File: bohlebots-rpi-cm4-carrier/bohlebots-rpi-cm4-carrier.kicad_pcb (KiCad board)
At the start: 2 copper layers, 132 x 132 mm, 41 parts, among them J1 SI-46001-F, J2 power_reference, J3 IO_Conn_02x05, J4 I2C_Conn_1x04, J5 pwr_connector, J6 pwr_connector, K1 Kicker, T1 Taster_LED, T2 Taster_LED, U1 Compute_Module_4_Connectors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

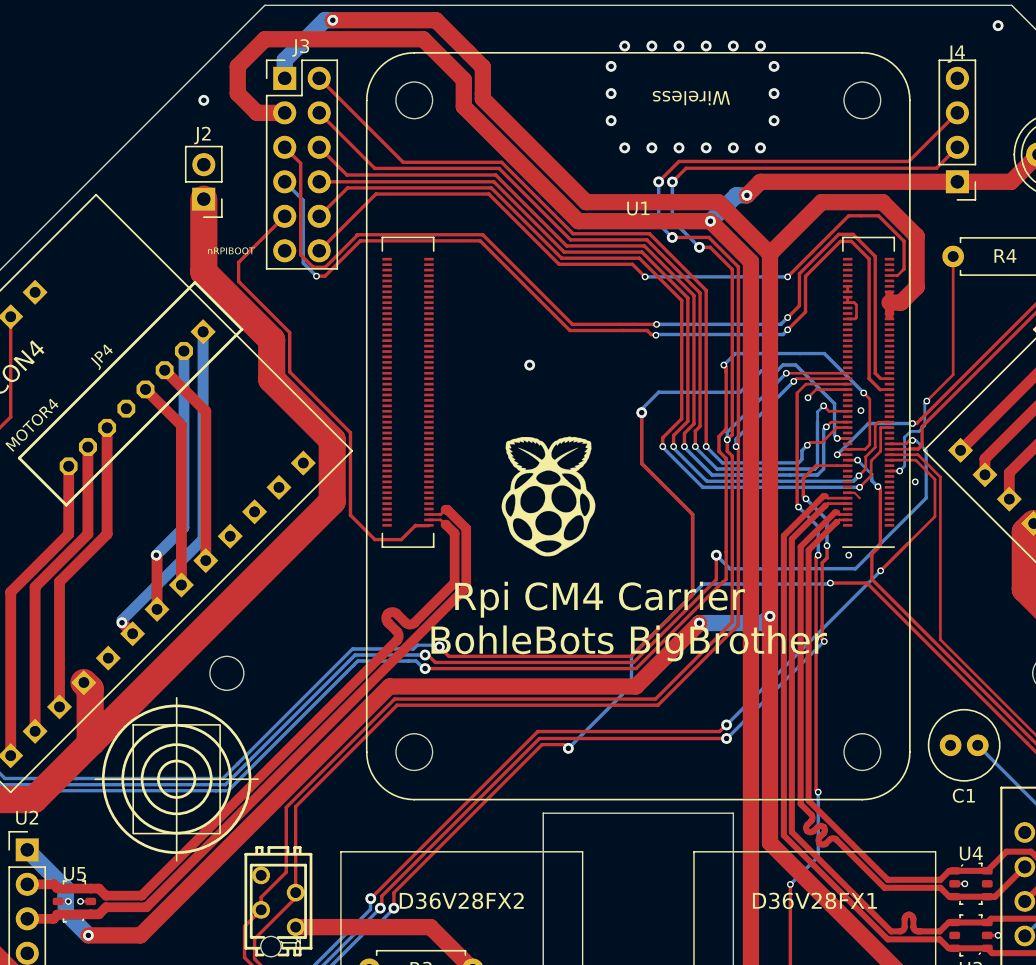
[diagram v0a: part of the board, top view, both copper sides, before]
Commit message: Added qr-c, fixed 'single connector footpring' issue, added compensation vias.
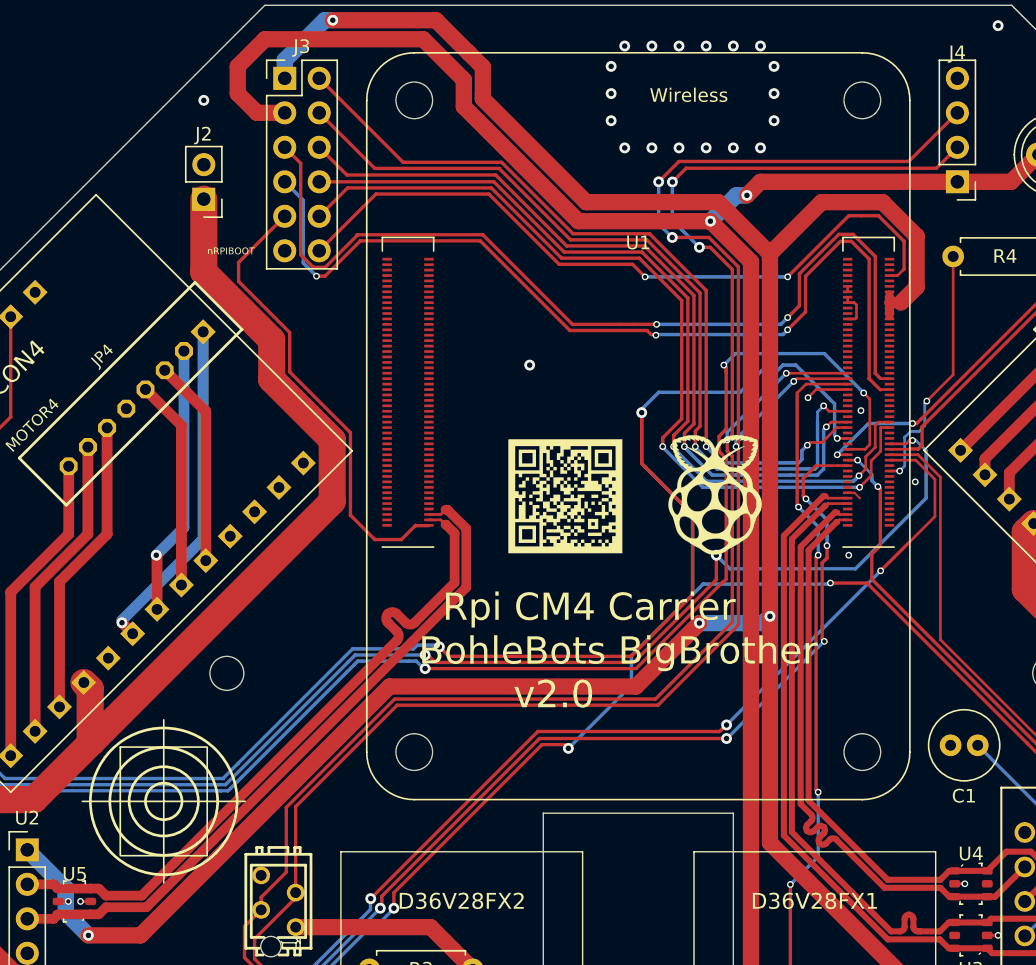
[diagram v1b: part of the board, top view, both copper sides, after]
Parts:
- added G***: LOGO, bohlebots-rpi-cm4-carrier:qr_code_bigbrother_org_small, F.Cu at (100.1, 75.7)
- added U7: Compute_Module_4_Connector_A, RPi_Compute_Module_4:Hirose-DF40C-100DS-0.4V(51), F.Cu at (122.5, 68.2)
- added U8: Compute_Module_4_Connector_B, RPi_Compute_Module_4:Hirose-DF40C-100DS-0.4V(51), F.Cu at (88.5, 68.2)
- moved G*** 12.3 mm to (111.2, 75.5)
- moved U1 2.50 mm to (105.5, 70.5)
- moved REF** 1.89 mm to (70.5, 98.1)
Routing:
- net Net-(U7-GPIO_VREF): track 0.00 -> 2.74 mm
- net Net-(U1A-GPIO_VREF): track 2.74 -> 0.00 mm
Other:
- board text added: "Rpi CM4 Carrier BohleBots BigBrother v2.0"
- board text removed: "Rpi CM4 Carrier BohleBots BigBrother"
